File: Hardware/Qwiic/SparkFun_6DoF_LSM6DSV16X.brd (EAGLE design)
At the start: 25.4 x 25.4 mm, 86 parts, among them J1 QWIIC_RIGHT_ANGLE, J2 QWIIC_RIGHT_ANGLE, P1 110pF, P2 110pF, U2 LSM6DSV16X

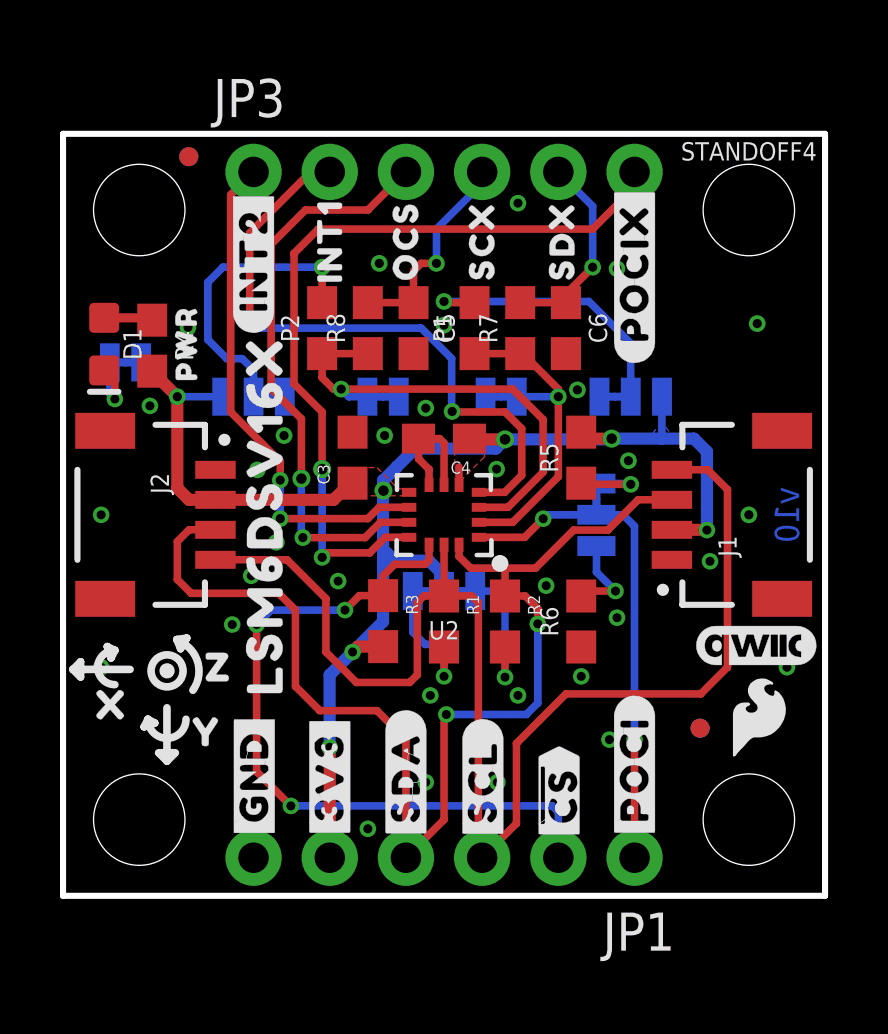
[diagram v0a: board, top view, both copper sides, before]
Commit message: Increases pad size, decreases paste size on footprint
* Also adds trestrict between ground pads to the footprint itself
* Fixes gyro silk on bottom
* Swaps PICO and CS on 1x1 header
* Improves ground pour
* Adds more notes to the filter section
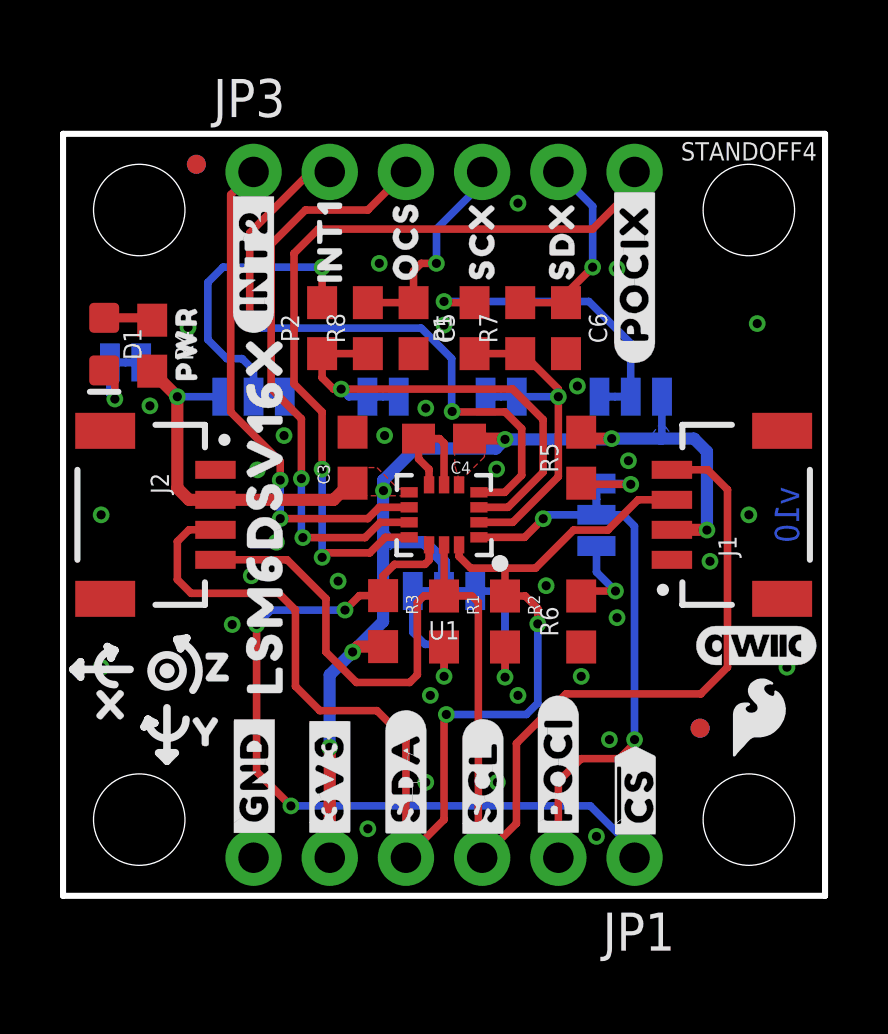
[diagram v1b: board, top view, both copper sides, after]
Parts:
- removed U$22: (no value), bot:#SCL#5
- added LOGO3: SFE_LOGO_NAME_FLAMEBLANK, SparkFun-Aesthetics:BLANK
- added U$48: (no value), pot:#SCLK#4
- R4: value 1k -> 4.7k
- U$16: device bot:#LED#11 -> pot:#LED#4
- U$23: device pot:#P1#4 -> pot:#PAD1#4
- U$30: device pot:#P2#4 -> pot:#PAD2#4
- moved U$18 2.54 mm to (16.5, 4.22)
- moved U$27 2.54 mm to (19.1, 3.35)
- moved U$3 2.54 mm to (19.1, 3.35)
- moved U$6 2.54 mm to (16.5, 4.22)
- moved FD1 0.36 mm to (4.45, 24.4)
- moved FID1 0.36 mm to (4.45, 24.4)
- moved U$37 0.18 mm to (20.8, 7.87)
- moved U$16 0.13 mm to (2.03, 19.3)
- moved U$19 0.13 mm to (14.0, 21.5)
- moved U$23 0.06 mm to (18.9, 15.1)
- moved U$30 0.06 mm to (6.22, 15.1)
- turned LOGO2 to 0 degrees
- renumbered U2 to U1
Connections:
- net SCL renamed SCL/SCLK
- net !CS!: now also JP1.1; no longer JP1.2
- net POCI/SA0: now also JP1.2; no longer JP1.1
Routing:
- net !CS!: track 24.6 -> 26.4 mm
- net POCI/SA0: track 16.7 -> 18.5 mm
- net 3.3V: track 49.8 -> 49.0 mm
- net GND: vias 32 -> 33
